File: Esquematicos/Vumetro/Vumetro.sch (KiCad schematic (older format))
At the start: 1 part

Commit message: se realiza esquematico en forma parcial
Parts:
- removed J?: AudioJack3_Ground_Switch, symbol Connector:AudioJack3_Ground_Switch
- added J?: AudioJack3_Ground, symbol Connector:AudioJack3_Ground
- added R? (x2): R, symbol Device:R
- added RV?: R_POT, symbol Device:R_POT
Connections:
- net labels added: +3.3V, GNDA
- wire segments 0 -> 15
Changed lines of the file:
@@
 EESchema Schematic File Version 4
+LIBS:Vumetro-cache
 EELAYER 26 0
 EELAYER END
@@
 $EndDescr
 $Comp
-L Connector:AudioJack3_Ground_Switch J?
-U 1 1 5BD06EAA
-P 2000 1850
-F 0 "J?" H 2004 2192 50  0000 C CNN
-F 1 "AudioJack3_Ground_Switch" H 2004 2101 50  0000 C CNN
-F 2 "" H 2000 1850 50  0001 C CNN
-F 3 "~" H 2000 1850 50  0001 C CNN
-	1    2000 1850
+L Device:R R?
+U 1 1 5BD08240
+P 1700 2950
+F 0 "R?" H 1770 2996 50  0000 L CNN
+F 1 "R" H 1770 2905 50  0000 L CNN
+F 2 "" V 1630 2950 50  0001 C CNN
+F 3 "~" H 1700 2950 50  0001 C CNN
+	1    1700 2950
 	1    0    0    -1
 $EndComp
+$Comp
+L Device:R R?
+U 1 1 5BD082FA
+P 1700 3400
+F 0 "R?" H 1770 3446 50  0000 L CNN
+F 1 "R" H 1770 3355 50  0000 L CNN
+F 2 "" V 1630 3400 50  0001 C CNN
+F 3 "~" H 1700 3400 50  0001 C CNN
+	1    1700 3400
+	1    0    0    -1
+$EndComp
+$Comp
+L power:GNDA #PWR?
+U 1 1 5BD08356
+P 1700 3700
+F 0 "#PWR?" H 1700 3450 50  0001 C CNN
+F 1 "GNDA" H 1705 3527 50  0000 C CNN
+F 2 "" H 1700 3700 50  0001 C CNN
+F 3 "" H 1700 3700 50  0001 C CNN
+	1    1700 3700
+	1    0    0    -1
+$EndComp
+Wire Wire Line
+	1700 3700 1700 3550
+$Comp
+L power:+3.3V #PWR?
+U 1 1 5BD083BF
+P 1700 2600
+F 0 "#PWR?" H 1700 2450 50  0001 C CNN
+F 1 "+3.3V" H 1715 2773 50  0000 C CNN
+F 2 "" H 1700 2600 50  0001 C CNN
+F 3 "" H 1700 2600 50  0001 C CNN
+	1    1700 2600
+	1    0    0    -1
+$EndComp
+Wire Wire Line
+	1700 2600 1700 2800
+$Comp
+L Connector:AudioJack3_Ground J?
+U 1 1 5BD08A54
+P 1800 1800
+F 0 "J?" H 1804 2142 50  0000 C CNN
+F 1 "AudioJack3_Ground" H 1804 2051 50  0000 C CNN
+F 2 "" H 1800 1800 50  0001 C CNN
+F 3 "~" H 1800 1800 50  0001 C CNN
+	1    1800 1800
+	1    0    0    -1
+$EndComp
+$Comp
+L power:GNDA #PWR?
+U 1 1 5BD08B01
+P 3650 1700
+F 0 "#PWR?" H 3650 1450 50  0001 C CNN
+F 1 "GNDA" H 3655 1527 50  0000 C CNN
+F 2 "" H 3650 1700 50  0001 C CNN
+F 3 "" H 3650 1700 50  0001 C CNN
+	1    3650 1700
+	1    0    0    -1
+$EndComp
+Wire Wire Line
+	2000 1700 3450 1700
+Wire Wire Line
+	2450 1900 2000 1900
+Wire Wire Line
+	2000 1800 2450 1800
+Wire Wire Line
+	2450 1800 2450 1900
+Wire Wire Line
+	1700 3100 1700 3150
+$Comp
+L Device:R_POT RV?
+U 1 1 5BD09203
+P 2850 2150
+F 0 "RV?" H 2780 2196 50  0000 R CNN
+F 1 "R_POT" H 2780 2105 50  0000 R CNN
+F 2 "" H 2850 2150 50  0001 C CNN
+F 3 "~" H 2850 2150 50  0001 C CNN
+	1    2850 2150
+	0    1    1    0
+$EndComp
+Wire Wire Line
+	2450 1900 2450 2150
+Wire Wire Line
+	2450 2150 2700 2150
+Connection ~ 2450 1900
+Wire Wire Line
+	3000 2150 3450 2150
+Wire Wire Line
+	3450 2150 3450 1700
+Connection ~ 3450 1700
+Wire Wire Line
+	3450 1700 3650 1700
+Wire Wire Line
+	2850 3150 2850 2300
+Connection ~ 1700 3150
+Wire Wire Line
+	1700 3150 1700 3250
+Wire Wire Line
+	1700 3150 2850 3150
 $EndSCHEMATC

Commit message: el capitan
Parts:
- added U?: MAX7219, symbol vumetro:MAX7219
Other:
- moved on the sheet: R?
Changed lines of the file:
@@
 L Device:R R?
 U 1 1 5BD08240
-P 1700 2950
-F 0 "R?" H 1770 2996 50  0000 L CNN
-F 1 "R" H 1770 2905 50  0000 L CNN
-F 2 "" V 1630 2950 50  0001 C CNN
-F 3 "~" H 1700 2950 50  0001 C CNN
-	1    1700 2950
+P 3400 2900
+F 0 "R?" H 3470 2946 50  0000 L CNN
+F 1 "R" H 3470 2855 50  0000 L CNN
+F 2 "" V 3330 2900 50  0001 C CNN
+F 3 "~" H 3400 2900 50  0001 C CNN
+	1    3400 2900
 	1    0    0    -1
 $EndComp
@@
 L Device:R R?
 U 1 1 5BD082FA
-P 1700 3400
-F 0 "R?" H 1770 3446 50  0000 L CNN
-F 1 "R" H 1770 3355 50  0000 L CNN
-F 2 "" V 1630 3400 50  0001 C CNN
-F 3 "~" H 1700 3400 50  0001 C CNN
-	1    1700 3400
+P 3400 3400
+F 0 "R?" H 3470 3446 50  0000 L CNN
+F 1 "R" H 3470 3355 50  0000 L CNN
+F 2 "" V 3330 3400 50  0001 C CNN
+F 3 "~" H 3400 3400 50  0001 C CNN
+	1    3400 3400
 	1    0    0    -1
 $EndComp
 $Comp
-L power:GNDA #PWR?
-U 1 1 5BD08356
-P 1700 3700
-F 0 "#PWR?" H 1700 3450 50  0001 C CNN
-F 1 "GNDA" H 1705 3527 50  0000 C CNN
-F 2 "" H 1700 3700 50  0001 C CNN
-F 3 "" H 1700 3700 50  0001 C CNN
-	1    1700 3700
+L power:+3.3V #PWR?
+U 1 1 5BD083BF
+P 3400 2550
+F 0 "#PWR?" H 3400 2400 50  0001 C CNN
+F 1 "+3.3V" H 3415 2723 50  0000 C CNN
+F 2 "" H 3400 2550 50  0001 C CNN
+F 3 "" H 3400 2550 50  0001 C CNN
+	1    3400 2550
 	1    0    0    -1
 $EndComp
 Wire Wire Line
-	1700 3700 1700 3550
-$Comp
-L power:+3.3V #PWR?
-U 1 1 5BD083BF
-P 1700 2600
-F 0 "#PWR?" H 1700 2450 50  0001 C CNN
-F 1 "+3.3V" H 1715 2773 50  0000 C CNN
-F 2 "" H 1700 2600 50  0001 C CNN
-F 3 "" H 1700 2600 50  0001 C CNN
-	1    1700 2600
-	1    0    0    -1
-$EndComp
-Wire Wire Line
-	1700 2600 1700 2800
+	3400 2550 3400 2750
 $Comp
 L Connector:AudioJack3_Ground J?
@@
 Wire Wire Line
 	2450 1800 2450 1900
-Wire Wire Line
-	1700 3100 1700 3150
 $Comp
 L Device:R_POT RV?
@@
 Wire Wire Line
 	2850 3150 2850 2300
-Connection ~ 1700 3150
+$Comp
+L vumetro:MAX7219 U?
+U 1 1 5BD0C6D8
+P 7200 2150
+F 0 "U?" H 7200 2315 50  0000 C CNN
+F 1 "MAX7219" H 7200 2224 50  0000 C CNN
+F 2 "" H 7200 2350 50  0001 C CNN
+F 3 "" H 7200 2350 50  0001 C CNN
+	1    7200 2150
+	1    0    0    -1
+$EndComp
 Wire Wire Line
-	1700 3150 1700 3250
+	3400 3050 3400 3150
 Wire Wire Line
-	1700 3150 2850 3150
+	2850 3150 3400 3150
+Wire Wire Line
+	3400 3150 3400 3250
+Connection ~ 3400 3150
+$Comp
+L power:GNDA #PWR?
+U 1 1 5BD0D7F2
+P 3400 3650
+F 0 "#PWR?" H 3400 3400 50  0001 C CNN
+F 1 "GNDA" H 3405 3477 50  0000 C CNN
+F 2 "" H 3400 3650 50  0001 C CNN
+F 3 "" H 3400 3650 50  0001 C CNN
+	1    3400 3650
+	1    0    0    -1
+$EndComp
+Wire Wire Line
+	3400 3550 3400 3650
 $EndSCHEMATC

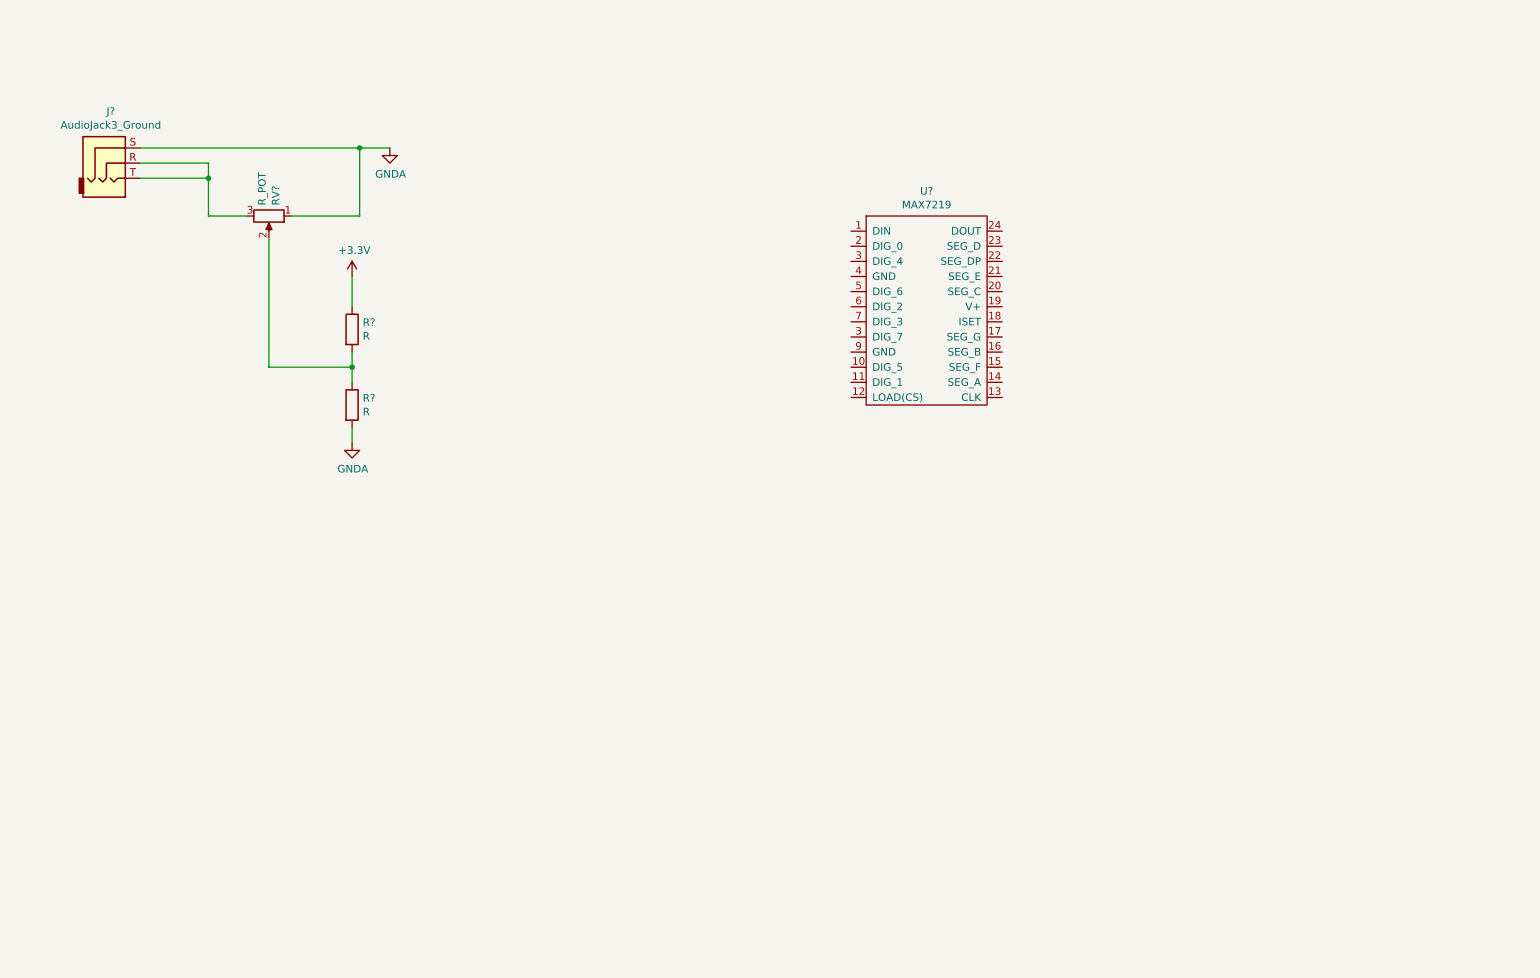
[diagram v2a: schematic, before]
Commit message: se agrega amplificador
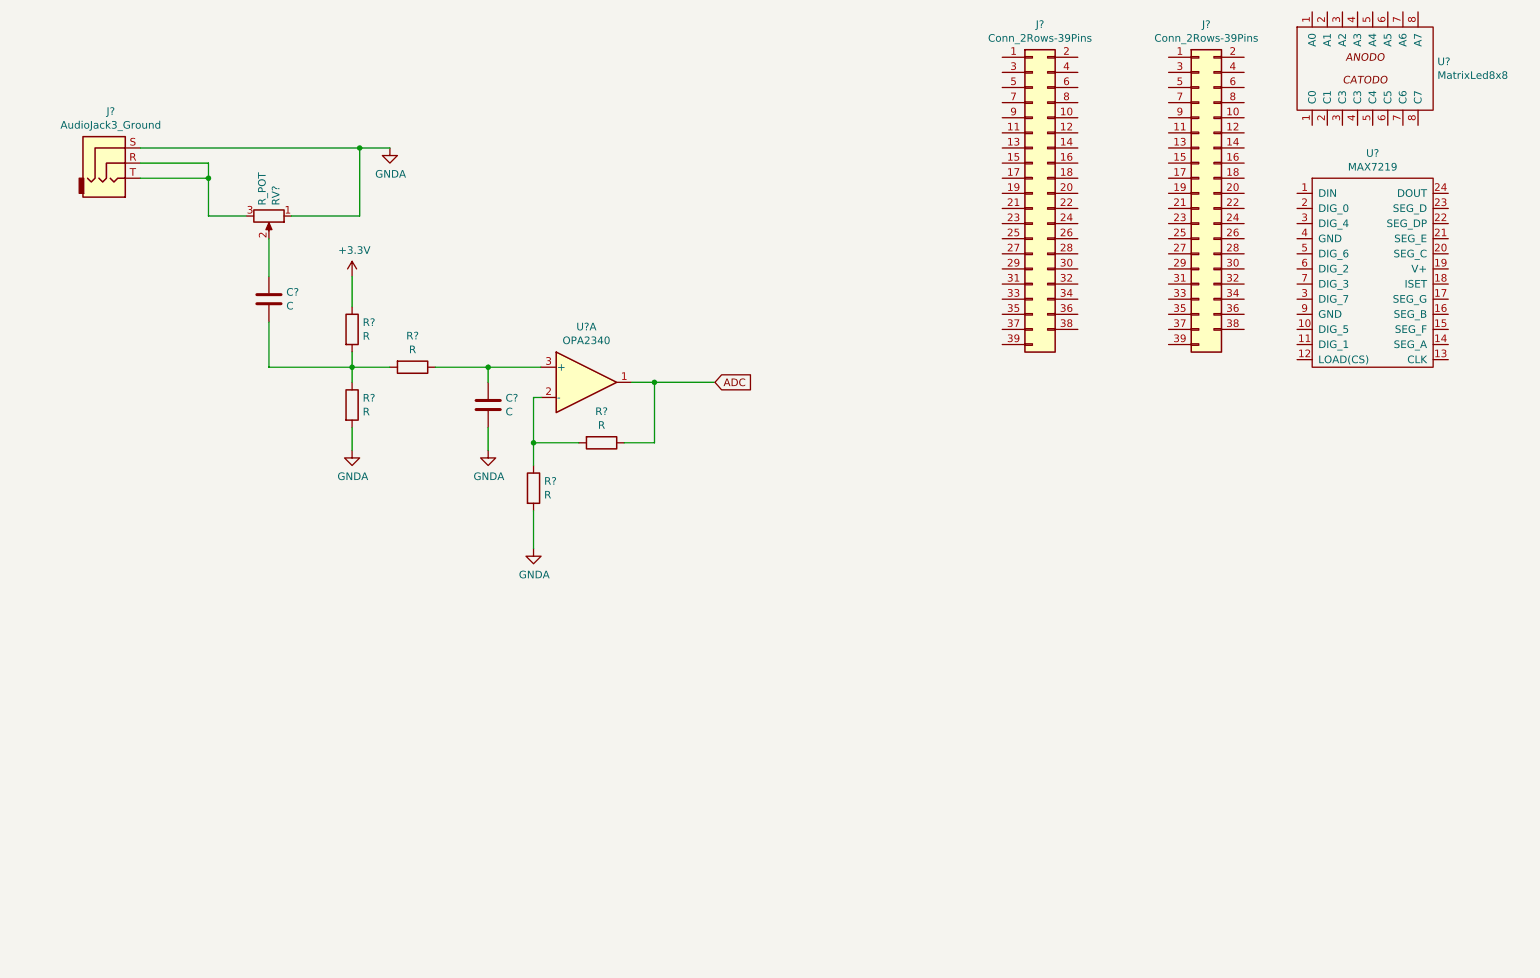
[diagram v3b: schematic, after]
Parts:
- added C? (x2): C, symbol Device:C
- added J? (x2): Conn_2Rows-39Pins, symbol Connector_Generic:Conn_2Rows-39Pins
- added R? (x3): R, symbol Device:R
- added U?: MatrixLed8x8, symbol vumetro:MatrixLed8x8
- added U?: OPA2340, symbol Amplifier_Operational:OPA2340
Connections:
- net GNDA: now also C?.2, R?.2
- net at R?.1, R?.2: now also C?.2, R?.2; no longer RV?.2
- new net: C?.1, RV?.2
- new net: C?.1, R?.1, U?.3 (+)
- new net: R?.1, R?.2, U?.2 (-)
- new net ADC: R?.1, U?.1
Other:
- moved on the sheet: U?
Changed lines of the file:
@@
 Wire Wire Line
 	3450 1700 3650 1700
-Wire Wire Line
-	2850 3150 2850 2300
 $Comp
 L vumetro:MAX7219 U?
 U 1 1 5BD0C6D8
-P 7200 2150
-F 0 "U?" H 7200 2315 50  0000 C CNN
-F 1 "MAX7219" H 7200 2224 50  0000 C CNN
-F 2 "" H 7200 2350 50  0001 C CNN
-F 3 "" H 7200 2350 50  0001 C CNN
-	1    7200 2150
+P 10150 1900
+F 0 "U?" H 10150 2065 50  0000 C CNN
+F 1 "MAX7219" H 10150 1974 50  0000 C CNN
+F 2 "" H 10150 2100 50  0001 C CNN
+F 3 "" H 10150 2100 50  0001 C CNN
+	1    10150 1900
 	1    0    0    -1
 $EndComp
@@
 L power:GNDA #PWR?
 U 1 1 5BD0D7F2
-P 3400 3650
-F 0 "#PWR?" H 3400 3400 50  0001 C CNN
-F 1 "GNDA" H 3405 3477 50  0000 C CNN
-F 2 "" H 3400 3650 50  0001 C CNN
-F 3 "" H 3400 3650 50  0001 C CNN
-	1    3400 3650
+P 3400 3700
+F 0 "#PWR?" H 3400 3450 50  0001 C CNN
+F 1 "GNDA" H 3405 3527 50  0000 C CNN
+F 2 "" H 3400 3700 50  0001 C CNN
+F 3 "" H 3400 3700 50  0001 C CNN
+	1    3400 3700
+	1    0    0    -1
+$EndComp
+$Comp
+L Device:C C?
+U 1 1 5BD1B29A
+P 4300 3400
+F 0 "C?" H 4415 3446 50  0000 L CNN
+F 1 "C" H 4415 3355 50  0000 L CNN
+F 2 "" H 4338 3250 50  0001 C CNN
+F 3 "~" H 4300 3400 50  0001 C CNN
+	1    4300 3400
+	1    0    0    -1
+$EndComp
+$Comp
+L power:GNDA #PWR?
+U 1 1 5BD1B343
+P 4300 3700
+F 0 "#PWR?" H 4300 3450 50  0001 C CNN
+F 1 "GNDA" H 4305 3527 50  0000 C CNN
+F 2 "" H 4300 3700 50  0001 C CNN
+F 3 "" H 4300 3700 50  0001 C CNN
+	1    4300 3700
 	1    0    0    -1
 $EndComp
 Wire Wire Line
-	3400 3550 3400 3650
+	4300 3550 4300 3700
+$Comp
+L Device:R R?
+U 1 1 5BD1B49E
+P 3800 3150
+F 0 "R?" V 3593 3150 50  0000 C CNN
+F 1 "R" V 3684 3150 50  0000 C CNN
+F 2 "" V 3730 3150 50  0001 C CNN
+F 3 "~" H 3800 3150 50  0001 C CNN
+	1    3800 3150
+	0    1    1    0
+$EndComp
+Wire Wire Line
+	3950 3150 4300 3150
+Wire Wire Line
+	4300 3150 4300 3250
+Text GLabel 5800 3250 2    50   Input ~ 0
+ADC
+Wire Wire Line
+	3400 3550 3400 3700
+$Comp
+L vumetro:MatrixLed8x8 U?
+U 1 1 5BD1C474
+P 10100 450
+F 0 "U?" H 10578 -229 50  0000 L CNN
+F 1 "MatrixLed8x8" H 10578 -320 50  0000 L CNN
+F 2 "" H 10000 450 50  0001 C CNN
+F 3 "" H 10000 450 50  0001 C CNN
+	1    10100 450
+	1    0    0    -1
+$EndComp
+$Comp
+L Connector_Generic:Conn_2Rows-39Pins J?
+U 1 1 5BD1C88D
+P 7900 2000
+F 0 "J?" H 7950 3117 50  0000 C CNN
+F 1 "Conn_2Rows-39Pins" H 7950 3026 50  0000 C CNN
+F 2 "" H 7900 2000 50  0001 C CNN
+F 3 "~" H 7900 2000 50  0001 C CNN
+	1    7900 2000
+	1    0    0    -1
+$EndComp
+$Comp
+L Connector_Generic:Conn_2Rows-39Pins J?
+U 1 1 5BD1CE86
+P 9000 2000
+F 0 "J?" H 9050 3117 50  0000 C CNN
+F 1 "Conn_2Rows-39Pins" H 9050 3026 50  0000 C CNN
+F 2 "" H 9000 2000 50  0001 C CNN
+F 3 "~" H 9000 2000 50  0001 C CNN
+	1    9000 2000
+	1    0    0    -1
+$EndComp
+$Comp
+L Amplifier_Operational:OPA2340 U?
+U 1 1 5BD1E25D
+P 4950 3250
+F 0 "U?" H 4950 3617 50  0000 C CNN
+F 1 "OPA2340" H 4950 3526 50  0000 C CNN
+F 2 "" H 4950 3250 50  0001 C CNN
+F 3 "http://www.ti.com/lit/ds/symlink/opa4340.pdf" H 4950 3250 50  0001 C CNN
+	1    4950 3250
+	1    0    0    -1
+$EndComp
+Wire Wire Line
+	3400 3150 3650 3150
+Wire Wire Line
+	4300 3150 4650 3150
+Connection ~ 4300 3150
+$Comp
+L Device:R R?
+U 1 1 5BD1FFCF
+P 4600 3950
+F 0 "R?" H 4670 3996 50  0000 L CNN
+F 1 "R" H 4670 3905 50  0000 L CNN
+F 2 "" V 4530 3950 50  0001 C CNN
+F 3 "~" H 4600 3950 50  0001 C CNN
+	1    4600 3950
+	1    0    0    -1
+$EndComp
+Wire Wire Line
+	4650 3350 4600 3350
+$Comp
+L Device:R R?
+U 1 1 5BD204D6
+P 5050 3650
+F 0 "R?" V 4843 3650 50  0000 C CNN
+F 1 "R" V 4934 3650 50  0000 C CNN
+F 2 "" V 4980 3650 50  0001 C CNN
+F 3 "~" H 5050 3650 50  0001 C CNN
+	1    5050 3650
+	0    1    1    0
+$EndComp
+Wire Wire Line
+	4600 3350 4600 3650
+Wire Wire Line
+	4900 3650 4600 3650
+Connection ~ 4600 3650
+Wire Wire Line
+	4600 3650 4600 3800
+Wire Wire Line
+	5200 3650 5400 3650
+Wire Wire Line
+	5400 3650 5400 3250
+Wire Wire Line
+	5400 3250 5250 3250
+$Comp
+L power:GNDA #PWR?
+U 1 1 5BD20C9D
+P 4600 4350
+F 0 "#PWR?" H 4600 4100 50  0001 C CNN
+F 1 "GNDA" H 4605 4177 50  0000 C CNN
+F 2 "" H 4600 4350 50  0001 C CNN
+F 3 "" H 4600 4350 50  0001 C CNN
+	1    4600 4350
+	1    0    0    -1
+$EndComp
+Wire Wire Line
+	4600 4100 4600 4350
+$Comp
+L Device:C C?
+U 1 1 5BD214BE
+P 2850 2700
+F 0 "C?" H 2965 2746 50  0000 L CNN
+F 1 "C" H 2965 2655 50  0000 L CNN
+F 2 "" H 2888 2550 50  0001 C CNN
+F 3 "~" H 2850 2700 50  0001 C CNN
+	1    2850 2700
+	1    0    0    -1
+$EndComp
+Wire Wire Line
+	2850 2300 2850 2550
+Wire Wire Line
+	2850 2850 2850 3150
+Wire Wire Line
+	5400 3250 5800 3250
+Connection ~ 5400 3250
 $EndSCHEMATC
